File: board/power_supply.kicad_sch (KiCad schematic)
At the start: 25 parts, among them J1 USB, U1 IP5306, U8 AZ1117-3.3

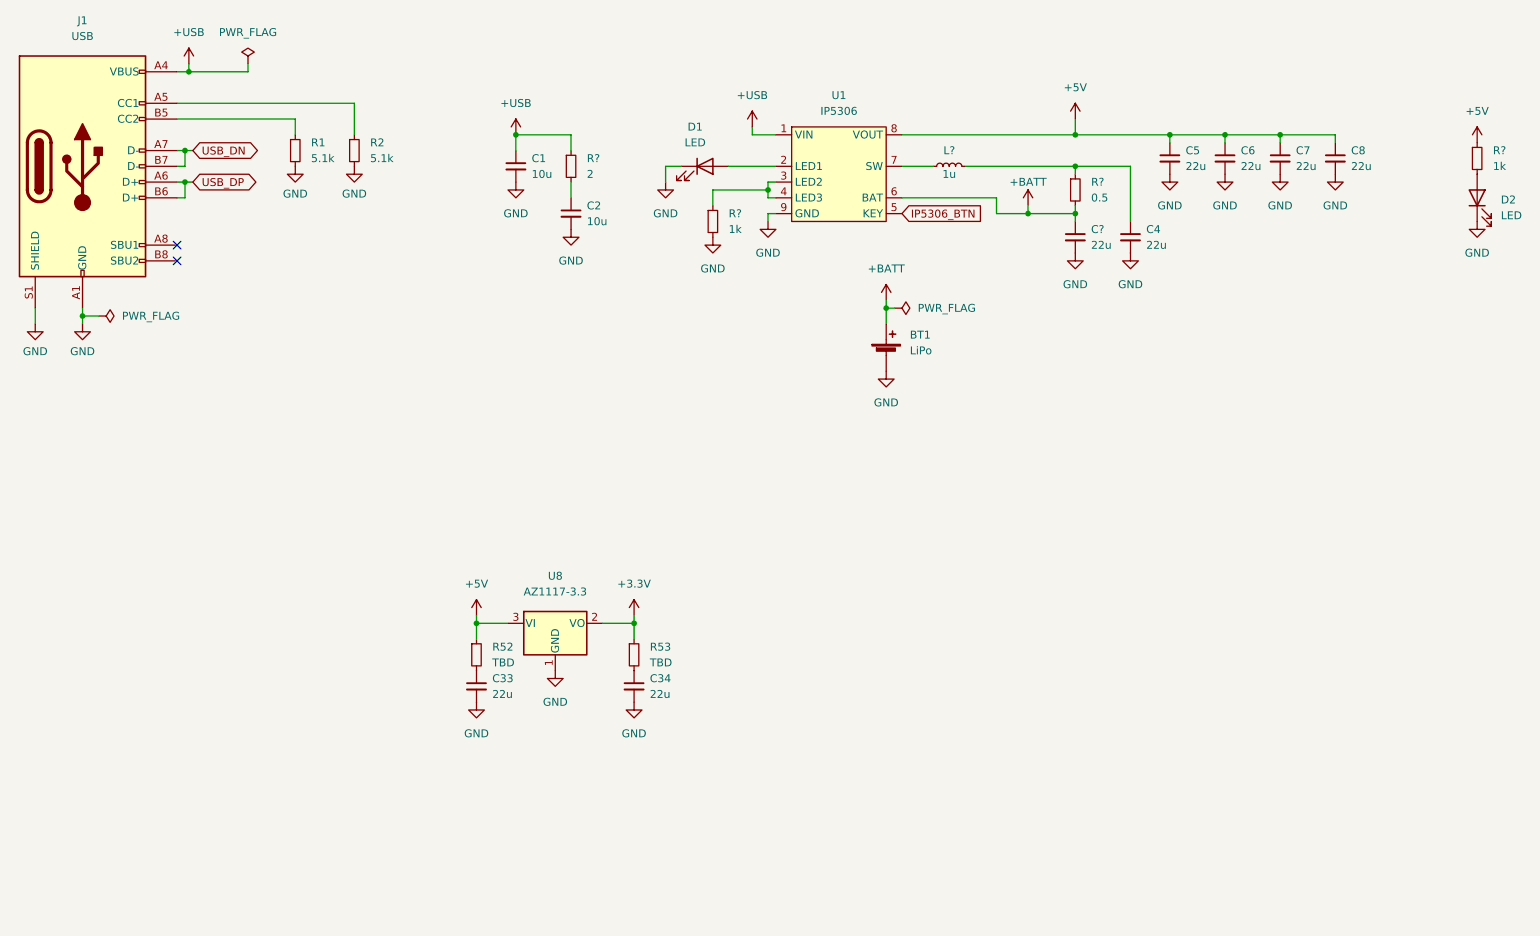
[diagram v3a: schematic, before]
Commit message: Added new ultrasonic circuit, changed the 3.3V regulator to a buck converter, and fixed some issues
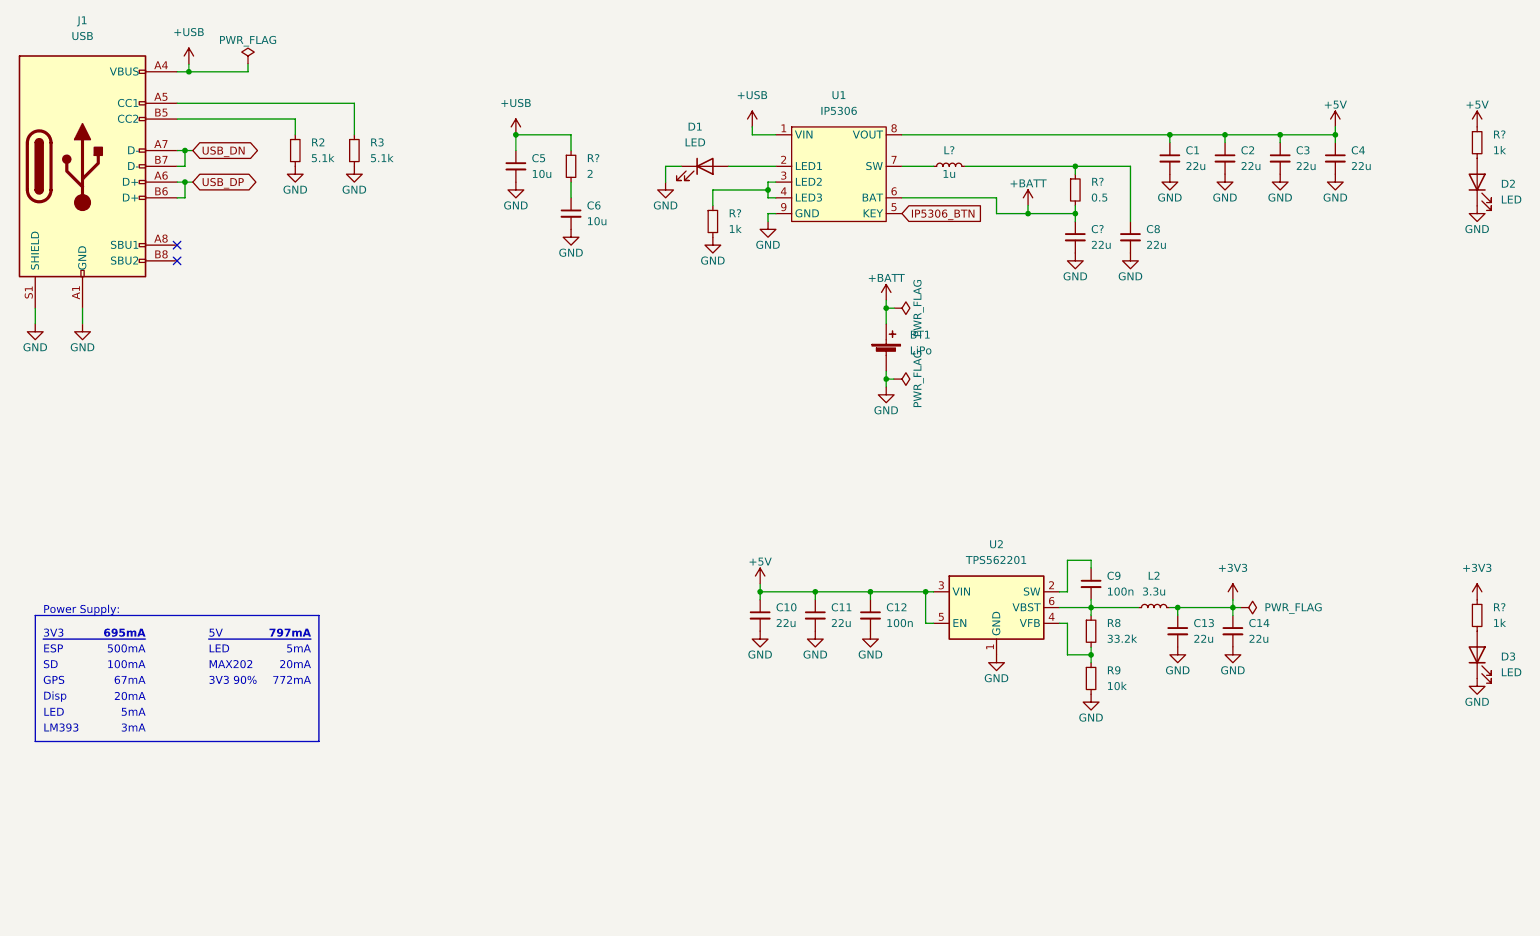
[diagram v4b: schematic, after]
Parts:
- removed C33, C34: 22u, Capacitor_SMD:C_1206_3216Metric, symbol Device:C_Small
- removed R52, R53: TBD, symbol Device:R_Small
- removed U8: AZ1117-3.3, symbol Regulator_Linear:AZ1117-3.3
- added C10, C11, C13, C14: 22u, Capacitor_SMD:C_1206_3216Metric, symbol Device:C_Small
- added C12, C9: 100n, Capacitor_SMD:C_0603_1608Metric, symbol Device:C_Small
- added D3: LED, LED_SMD:LED_0603_1608Metric, symbol Device:LED
- added L2: 3.3u, Inductor_SMD:L_Vishay_IFSC-1515AH_4x4x1.8mm, symbol Device:L_Small
- added R8: 33.2k, Resistor_SMD:R_0603_1608Metric, symbol Device:R_Small
- added R9: 10k, Resistor_SMD:R_0603_1608Metric, symbol Device:R_Small
- added R?: 1k, Resistor_SMD:R_0603_1608Metric, symbol Device:R_Small
- added U2: TPS562201, Package_TO_SOT_SMD:SOT-23-6, symbol Regulator_Switching:TPS562200
- BT1: footprint (none) -> Connector_JST:JST_XH_B2B-XH-A_1x02_P2.50mm_Vertical; JLC_PN (none) -> C2979476; MPN (none) -> HC-XH-2A-M; Manufacturer (none) -> HCTL
- J1: footprint (none) -> OBSPro:TYPE-C-31-M-12
- renumbered C5 to C1, C6 to C2, C7 to C3, C8 to C4, C1 to C5, C2 to C6, C4 to C8, R1 to R2, R2 to R3
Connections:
- net +5V: now also C10.1, C11.1, C12.1, U2.3 (VIN), U2.5 (EN)
- net GND: now also C10.2, C11.2, C12.2, C13.2, C14.2, D3.1 (K), R9.2, U2.1 (GND)
- new net: D3.2 (A), R?.2
- new net: C9.2, L2.1, R8.1, U2.6 (VBST)
- new net: R8.2, R9.1, U2.4 (VFB)
- new net: C9.1, U2.2 (SW)
- new net +3V3: C13.1, C14.1, L2.2, R?.1
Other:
- note added: "100mA"
- note added: "20mA"
- note added: "3V3"
- note added: "3V3 90%"
- note added: "3mA"
- note added: "500mA"
- note added: "5V"
- note added: "5mA"
- note added: "67mA"
- note added: "695mA"
- note added: "772mA"
- note added: "797mA"
- note added: "Disp"
- note added: "ESP"
- note added: "GPS"
- note added: "LED"
- note added: "LM393"
- note added: "MAX202"
- note added: "Power Supply:"
- note added: "SD"
- moved on the sheet: D2, R?

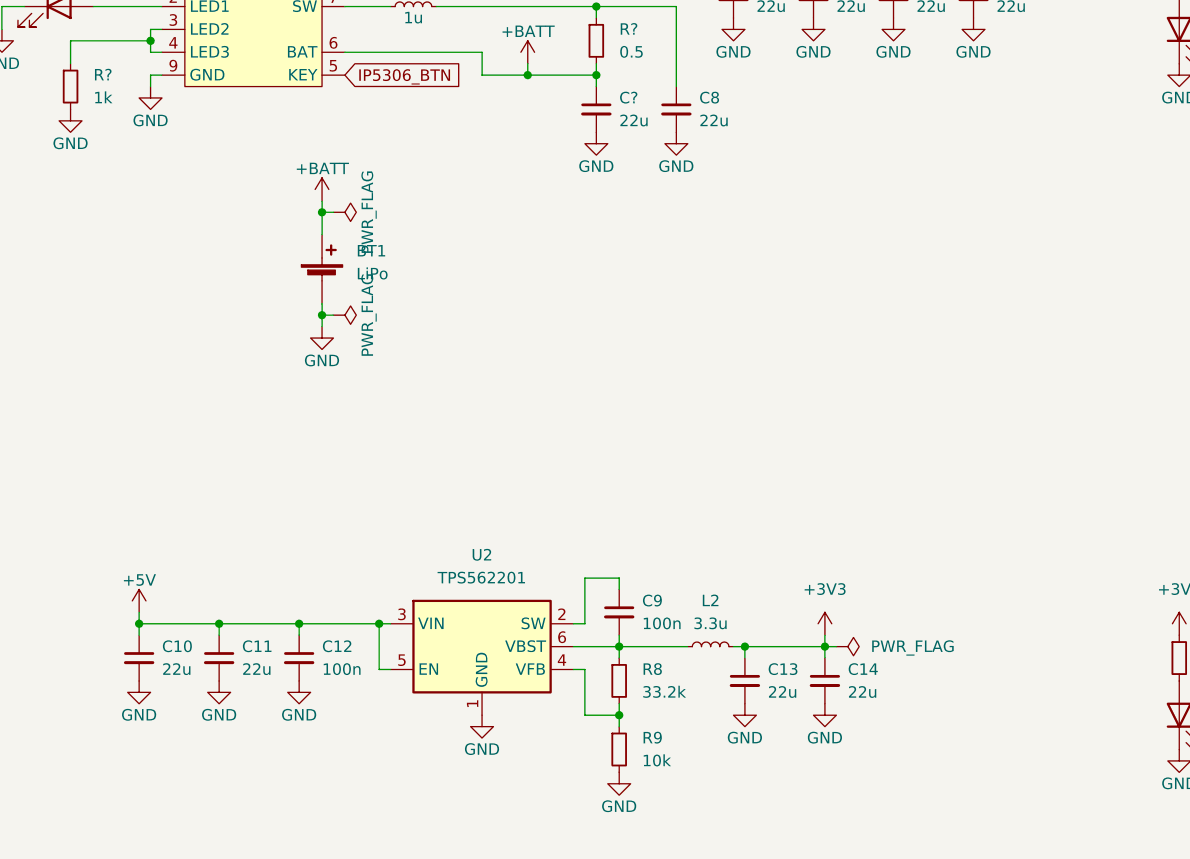
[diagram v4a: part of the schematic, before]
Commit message: First placement of parts, fixed a few bugs in the schematic
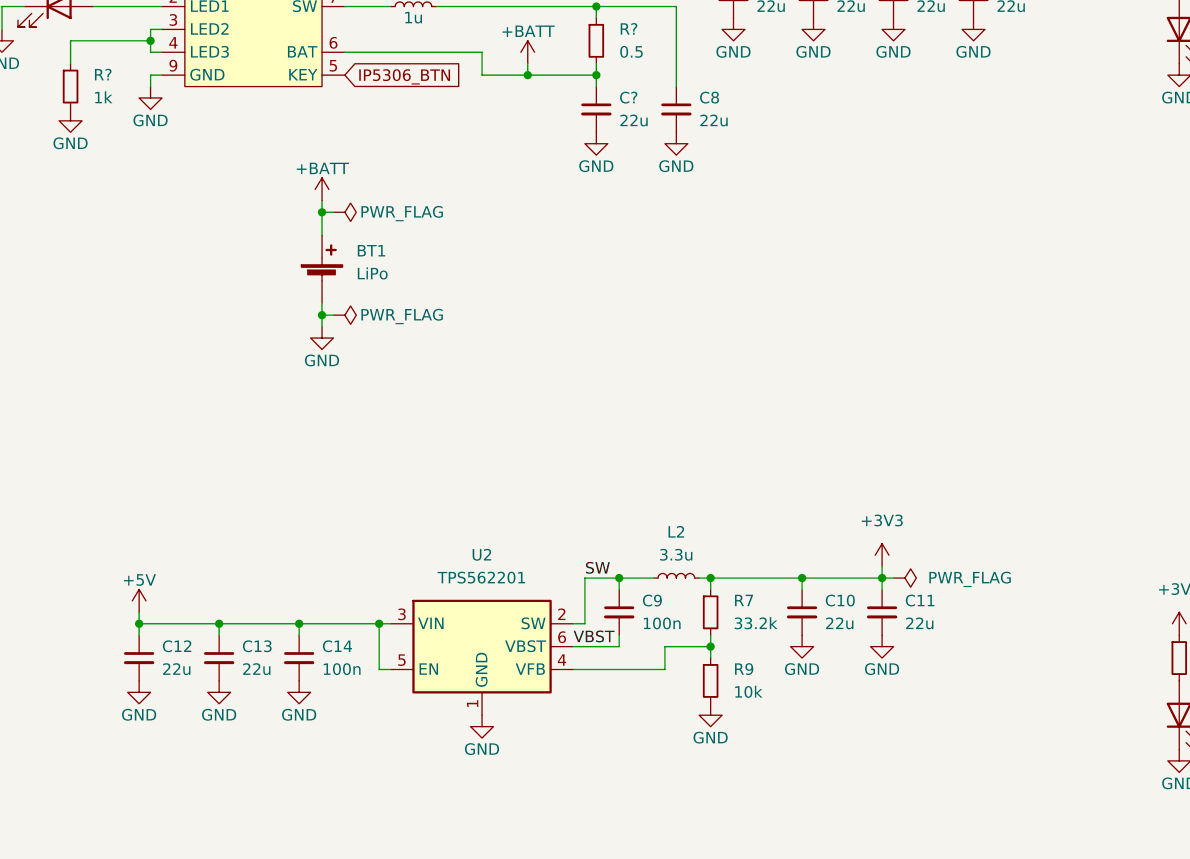
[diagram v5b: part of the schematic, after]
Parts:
- renumbered C13 to C10, C14 to C11, C10 to C12, C11 to C13, C12 to C14, R8 to R7
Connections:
- net +3V3: now also R7.1
- net VBST: now reaches C9.2, U2.6 (VBST)
- net VBST: no longer L2.1, R7.1
- net SW: now reaches C9.1, U2.2 (SW)
- net SW: now also L2.1
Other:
- moved on the sheet: C10, C11, L2, R7, R9

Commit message: Swapped footprints of connectors, optimized placement
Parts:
- BT1: footprint Connector_JST:JST_XH_B2B-XH-A_1x02_P2.50mm_Vertical -> OBSPro:PSS-254-2W
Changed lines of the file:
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@@
       (effects (font (size 1.27 1.27)) (justify left))
     )
-    (property "Footprint" "Connector_JST:JST_XH_B2B-XH-A_1x02_P2.50mm_Vertical" (id 2) (at 166.37 70.866 90)
+    (property "Footprint" "OBSPro:PSS-254-2W" (id 2) (at 166.37 70.866 90)
       (effects (font (size 1.27 1.27)) hide)
     )

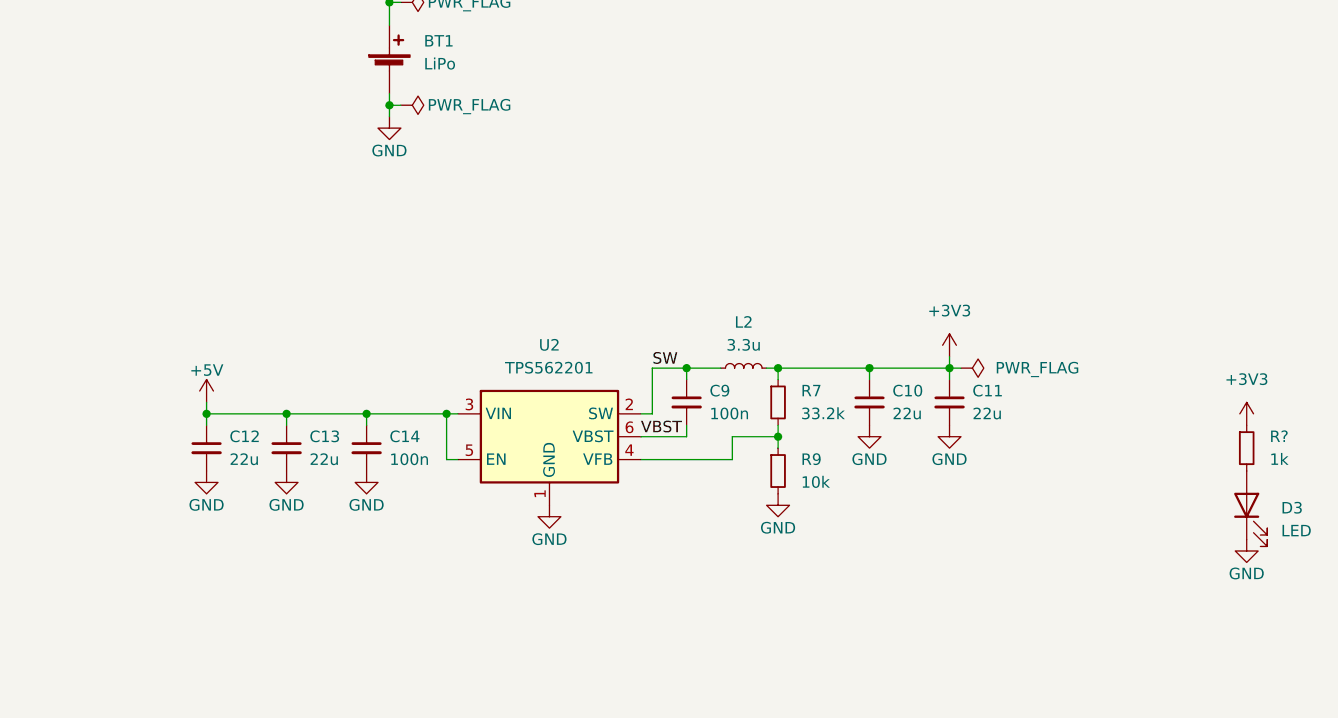
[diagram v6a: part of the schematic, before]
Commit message: Everything routed, a few changes in the components, first prototypes ordered
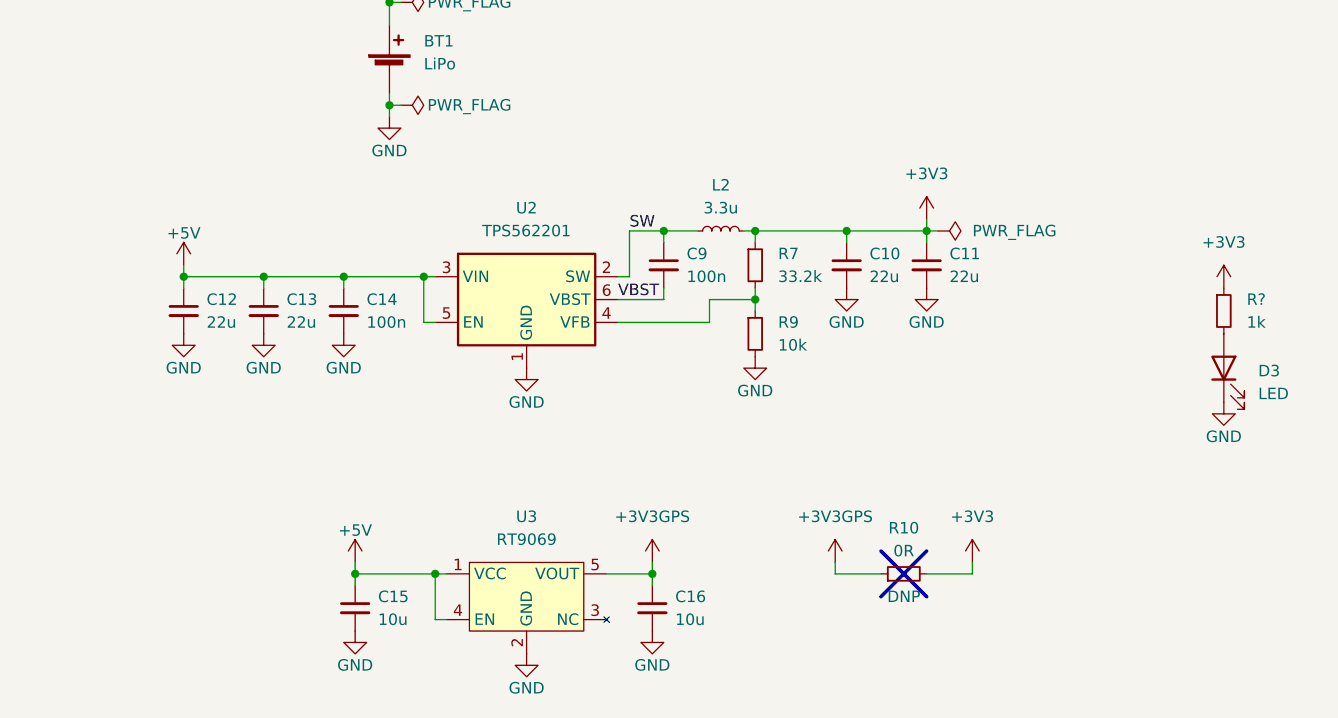
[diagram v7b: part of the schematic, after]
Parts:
- added C15, C16: 10u, Capacitor_SMD:C_0603_1608Metric, symbol Device:C_Small
- added R10: 0R, Resistor_SMD:R_0603_1608Metric, symbol Device:R_Small
- added U3: RT9069, Package_TO_SOT_SMD:SOT-23-5, symbol OBSPro:RT9069
- BT1, L2, R7, U2: JLC_BasicPart (none) -> no
- D1, D2, D3: JLC_PN C2286 -> C72043; MPN KT-0603R -> 19-217/GHC-YR1S2/3T; Manufacturer Hubei KENTO Elec -> Everlight Elec
- R9: JLC_BasicPart (none) -> yes
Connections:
- net +3V3: now also R10.2
- net +5V: now also C15.1, U3.1 (VCC), U3.4 (EN)
- net GND: now also C15.2, C16.2, U3.2 (GND)
- new net +3V3GPS: C16.1, R10.1, U3.5 (VOUT)
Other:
- moved on the sheet: C10, C11, C12, C13, C14, C9, D3, L2, R7, R9, R?, U2

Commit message: Fixed ERC/DRC errors, last cleanup before production data export
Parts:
- J1: symbol Connector:USB_C_Receptacle_USB2.0 -> OBSPro:USB_C_Receptacle_USB2.0
- R10: JLC_BasicPart (none) -> yes; JLC_PN (none) -> C21189; MPN (none) -> 0603WAF0000T5E; Manufacturer (none) -> UNI-ROYAL(Uniroyal Elec)
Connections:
- net +USB: no longer J1.A9 (VBUS), J1.B9 (VBUS)
- net GND: no longer J1.A12 (GND), J1.B12 (GND)
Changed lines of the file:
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@@
     )
     (property "DNP" "DNP" (id 8) (at 223.52 130.81 90))
+    (property "JLC_BasicPart" "yes" (id 9) (at 223.52 128.27 0)
+      (effects (font (size 1.27 1.27)) hide)
+    )
+    (property "JLC_PN" "C21189" (id 10) (at 223.52 128.27 0)
+      (effects (font (size 1.27 1.27)) hide)
+    )
+    (property "MPN" "0603WAF0000T5E" (id 11) (at 223.52 128.27 0)
+      (effects (font (size 1.27 1.27)) hide)
+    )
+    (property "Manufacturer" "UNI-ROYAL(Uniroyal Elec)" (id 12) (at 223.52 128.27 0)
+      (effects (font (size 1.27 1.27)) hide)
+    )
     (pin "1")
     (pin "2")
@@
     (pin "1")
   )
-  (symbol (lib_id "Connector:USB_C_Receptacle_USB2.0") (at 36.83 41.91 0) (unit 1)
+  (symbol (lib_id "OBSPro:USB_C_Receptacle_USB2.0") (at 36.83 41.91 0) (unit 1)
     (in_bom yes) (on_board yes) (fields_autoplaced)
     (property "Reference" "J1" (id 0) (at 36.83 18.415 0))
@@
     )
     (pin "A1")
-    (pin "A12")
     (pin "A4")
     (pin "A5")
@@
     (pin "A7")
     (pin "A8")
-    (pin "A9")
     (pin "B1")
-    (pin "B12")
     (pin "B4")
     (pin "B5")
@@
     (pin "B7")
     (pin "B8")
-    (pin "B9")
     (pin "S1")
   )
